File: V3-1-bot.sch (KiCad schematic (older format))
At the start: 12 parts, among them J1 PowerPole, J2 Conn_01x12_Female, J3 Conn_01x12_Female, J4 Conn_01x03_Female, J5 Conn_01x03_Female, J6 Conn_01x03_Female, J7 Conn_01x03_Female, J8 Conn_01x03_Female, J9 Conn_01x03_Female, U1 Teensy4.0-Tall-Dog-Breakout

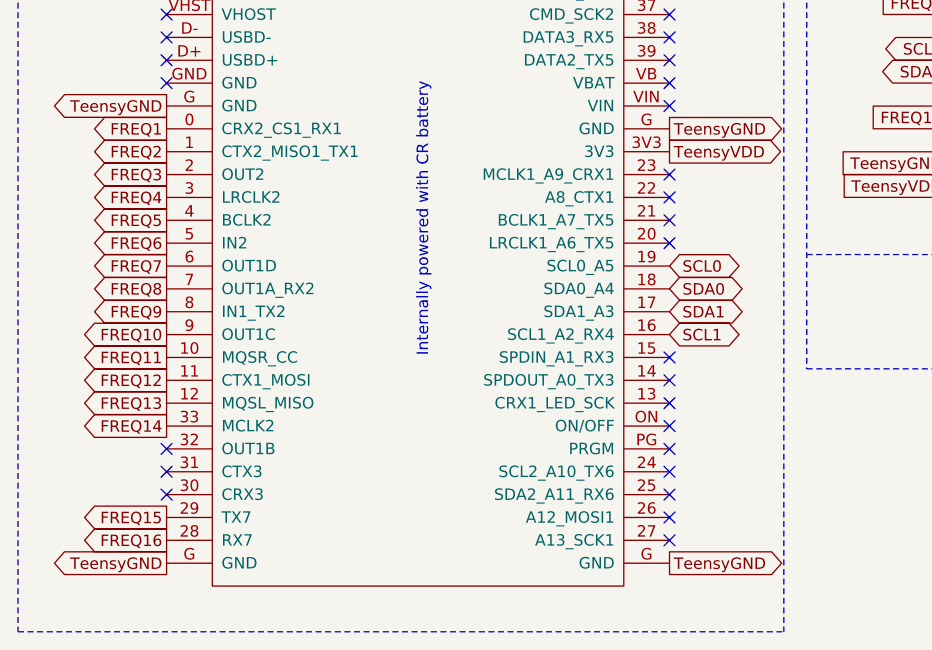
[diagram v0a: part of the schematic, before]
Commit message: Add bottom PCB WIP
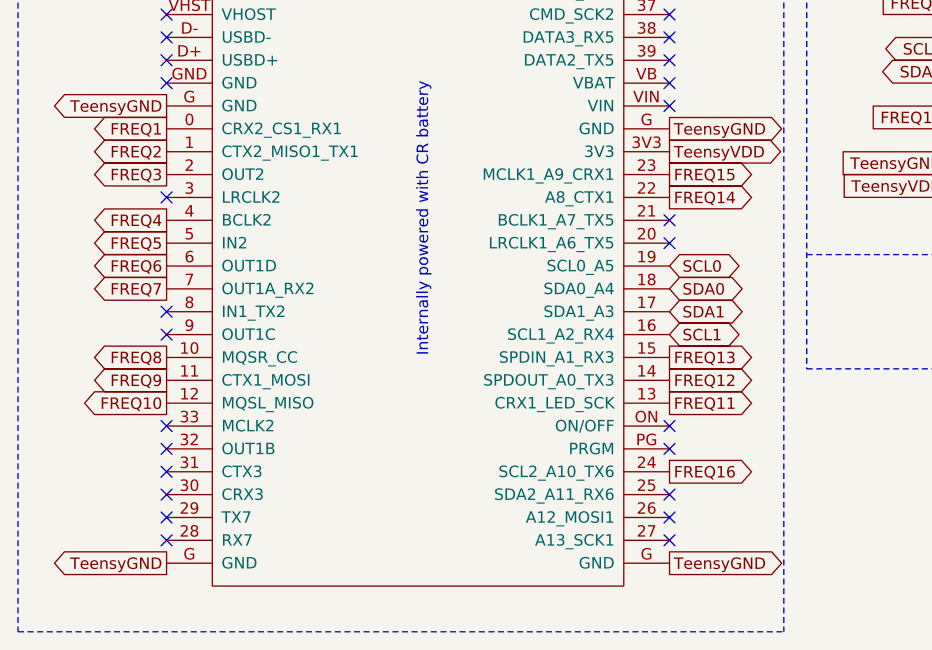
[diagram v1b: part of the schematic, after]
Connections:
- net FREQ10: now also U1.12 (MQSL_MISO); no longer U1.9 (OUT1C)
- net FREQ11: now also U1.13 (CRX1_LED_SCK); no longer U1.10 (MQSR_CC)
- net FREQ12: now also U1.14 (SPDOUT_A0_TX3); no longer U1.11 (CTX1_MOSI)
- net FREQ13: now also U1.15 (SPDIN_A1_RX3); no longer U1.12 (MQSL_MISO)
- net FREQ14: now also U1.22 (A8_CTX1); no longer U1.33 (MCLK2)
- net FREQ15: now also U1.23 (MCLK1_A9_CRX1); no longer U1.29 (TX7)
- net FREQ16: now also U1.24 (SCL2_A10_TX6); no longer U1.28 (RX7)
- net FREQ4: now also U1.4 (BCLK2); no longer U1.3 (LRCLK2)
- net FREQ5: now also U1.5 (IN2); no longer U1.4 (BCLK2)
- net FREQ6: now also U1.6 (OUT1D); no longer U1.5 (IN2)
- net FREQ7: now also U1.7 (OUT1A_RX2); no longer U1.6 (OUT1D)
- net FREQ8: now also U1.10 (MQSR_CC); no longer U1.7 (OUT1A_RX2)
- net FREQ9: now also U1.11 (CTX1_MOSI); no longer U1.8 (IN1_TX2)
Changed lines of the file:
@@
 Comment4 ""
 $EndDescr
-Text GLabel 1300 4750 0    50   Output ~ 0
+Text GLabel 1300 5050 0    50   Output ~ 0
 FREQ8
 Text GLabel 1300 4050 0    50   Output ~ 0
@@
 Text GLabel 1300 4250 0    50   Output ~ 0
 FREQ3
-Text GLabel 1300 4350 0    50   Output ~ 0
+Text GLabel 1300 4450 0    50   Output ~ 0
 FREQ4
-Text GLabel 1300 4450 0    50   Output ~ 0
+Text GLabel 1300 4550 0    50   Output ~ 0
 FREQ5
-Text GLabel 1300 4550 0    50   Output ~ 0
+Text GLabel 1300 4650 0    50   Output ~ 0
 FREQ6
-Text GLabel 1300 4650 0    50   Output ~ 0
+Text GLabel 1300 4750 0    50   Output ~ 0
 FREQ7
-Text GLabel 1300 4850 0    50   Output ~ 0
+Text GLabel 1300 5150 0    50   Output ~ 0
 FREQ9
-Text GLabel 1300 4950 0    50   Output ~ 0
+Text GLabel 1300 5250 0    50   Output ~ 0
 FREQ10
-Text GLabel 1300 5050 0    50   Output ~ 0
+Text GLabel 3500 5250 2    50   Output ~ 0
 FREQ11
 Text GLabel 3500 4950 2    50   BiDi ~ 0
@@
 Text GLabel 3500 4650 2    50   BiDi ~ 0
 SCL0
-Text GLabel 1300 5150 0    50   Output ~ 0
+Text GLabel 3500 5150 2    50   Output ~ 0
 FREQ12
-Text GLabel 1300 5250 0    50   Output ~ 0
+Text GLabel 3500 5050 2    50   Output ~ 0
 FREQ13
-Text GLabel 1300 5350 0    50   Output ~ 0
+Text GLabel 3500 4350 2    50   Output ~ 0
 FREQ14
-Text GLabel 1300 5750 0    50   Output ~ 0
+Text GLabel 3500 4250 2    50   Output ~ 0
 FREQ15
-Text GLabel 1300 5850 0    50   Output ~ 0
+Text GLabel 3500 5550 2    50   Output ~ 0
 FREQ16
 Text GLabel 3500 4150 2    50   Output ~ 0
@@
 NoConn ~ 3500 5750
 NoConn ~ 3500 5650
-NoConn ~ 3500 5550
 NoConn ~ 3500 5450
 NoConn ~ 3500 5350
-NoConn ~ 3500 5250
-NoConn ~ 3500 5150
-NoConn ~ 3500 5050
 NoConn ~ 3500 4550
-NoConn ~ 3500 4450
-NoConn ~ 3500 4350
-NoConn ~ 3500 4250
 NoConn ~ 3500 3950
 NoConn ~ 3500 3850
@@
 	-1   0    0    1
 $EndComp
+NoConn ~ 1300 5350
+NoConn ~ 1300 5850
+NoConn ~ 1300 5750
+NoConn ~ 1300 4950
+NoConn ~ 1300 4850
+NoConn ~ 1300 4350
+NoConn ~ 3500 4450
 $EndSCHEMATC

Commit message: Done BOT v3.1
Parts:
- U1: footprint Teensy:TallDogTeensy4.0Breakout -> HART:TallDogTeensy4.0Breakout
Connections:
- net GND: no longer J5.2 (Pin_2)
- no-connect marks 33 -> 34
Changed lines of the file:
@@
 GND
 NoConn ~ 8250 1650
-Text GLabel 8200 2750 2    50   Input ~ 0
-TeensyGND
 Text GLabel 8250 1550 2    50   Input ~ 0
 TeensyVDD
@@
 F 0 "U1" H 2400 6215 50  0000 C CNN
 F 1 "Teensy4.0-Tall-Dog-Breakout" H 2400 6124 50  0000 C CNN
-F 2 "Teensy:TallDogTeensy4.0Breakout" H 2400 3100 50  0001 C CNN
+F 2 "HART:TallDogTeensy4.0Breakout" H 2400 3100 50  0001 C CNN
 F 3 "" H 2400 3100 50  0001 C CNN
 	1    2400 4600
@@
 NoConn ~ 1300 4350
 NoConn ~ 3500 4450
+NoConn ~ 8200 2750
 $EndSCHEMATC

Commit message: Cleanup symbols and libraries and add separate submodule for kicad-libaries
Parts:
- R1, R2: symbol v3-rescue:R-Device -> pspice:R
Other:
- moved on the sheet: J4, J5, J6, J7, J8, J9
